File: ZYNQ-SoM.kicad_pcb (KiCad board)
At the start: 6 copper layers, 50 x 40 mm, 173 parts, among them IC501 TPS51206DSQR, J401 AXK500137YG, J402 AXK500137YG, Q201 MMBT3904, U201 xc7z010clg400, U202 W25Q256FVEI, U301 MT41K256M16TW-107_P, U501 TPS62130ARGTR, U502 TPS62130ARGTR, U503 SPX3819M5-L-3-3, U504 TPS62130ARGTR, U701 33.3333MHz

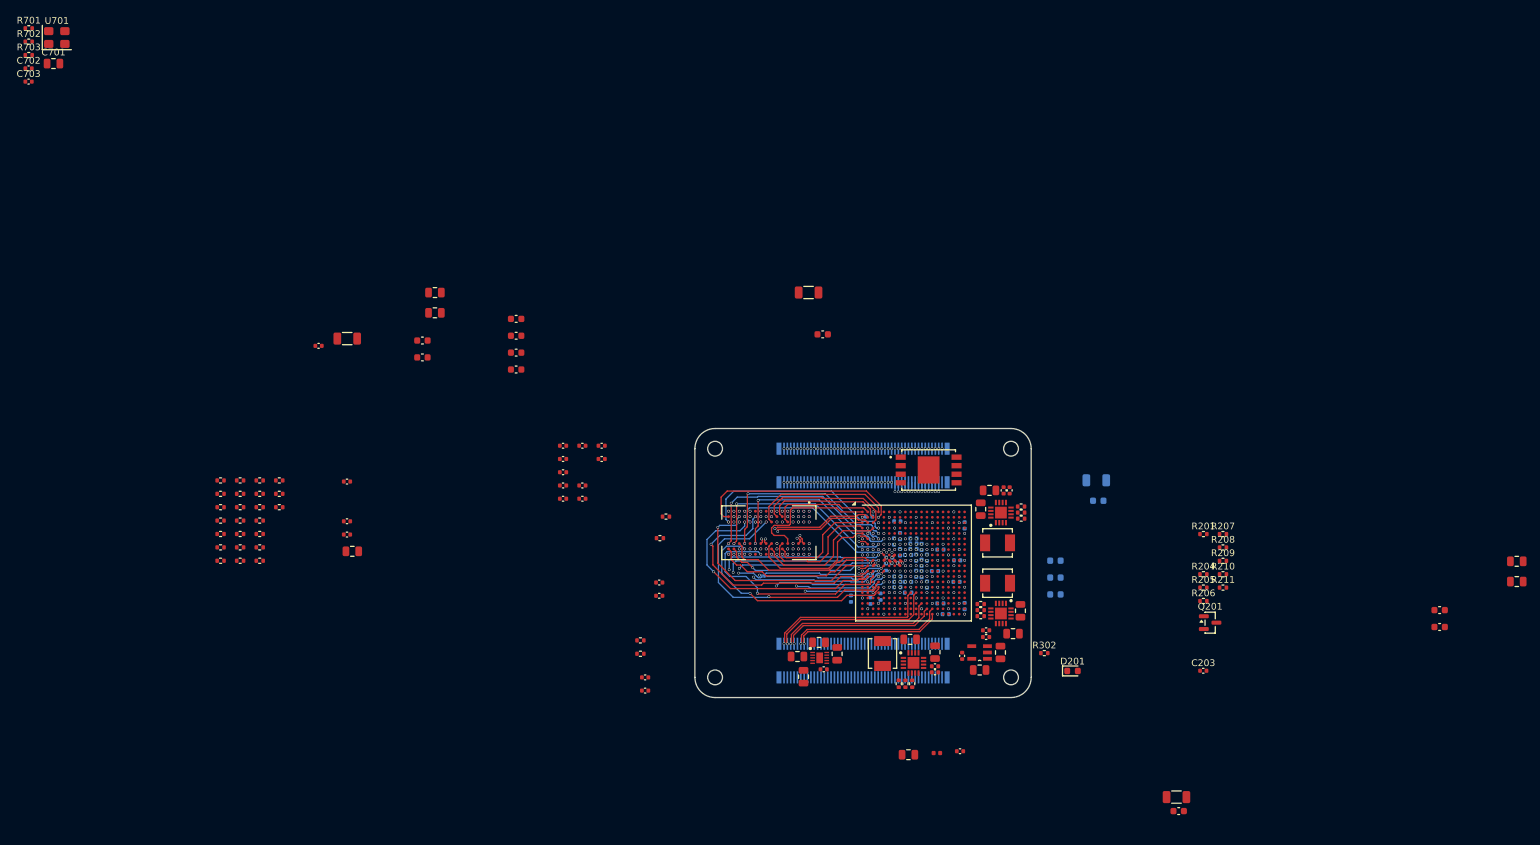
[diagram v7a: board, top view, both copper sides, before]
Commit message: layout: route mio and some io
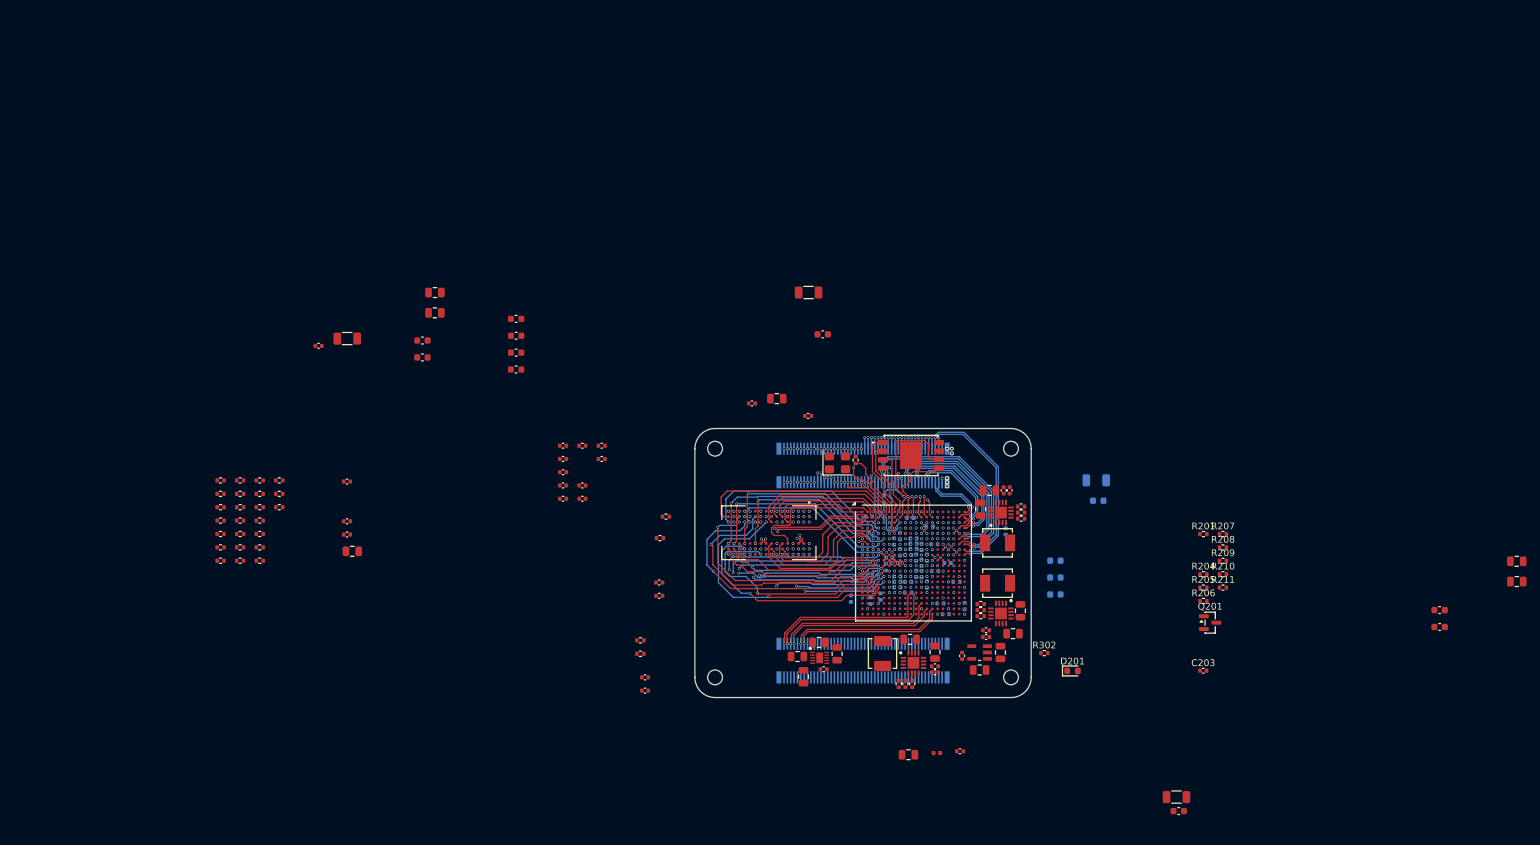
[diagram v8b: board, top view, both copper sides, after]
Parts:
- R701, R703: moved to B.Cu
- moved R703 151.2 mm to (134.9, 74.6)
- moved R701 145.1 mm to (128.1, 70.5), turned to -90 degrees
- moved R702 137.8 mm to (123.9, 64.7), turned to -90 degrees
- moved U701 132.2 mm to (121.2, 65.1)
- moved C703 126.1 mm to (116.8, 58.1)
- moved C701 118.5 mm to (112.2, 55.6)
- moved C702 118.5 mm to (108.5, 56.3)
- moved C565 6.17 mm to (146.2, 75.3)
- moved U202 3.40 mm to (132.1, 64.0)
- moved C551 1.96 mm to (132.0, 73.3)
- moved C559 1.48 mm to (137.6, 80.0)
- moved C571 1.20 mm to (135.6, 77.2)
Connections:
- J402 pad 10: unconnected-(J402-Pad10) -> GND
- J402 pad 100: unconnected-(J402-Pad100) -> GND
- J402 pad 11: unconnected-(J402-Pad11) -> PL_B35_IO1_N
- J402 pad 13: unconnected-(J402-Pad13) -> PL_B35_IO1_P
- J402 pad 15: unconnected-(J402-Pad15) -> GND
- J402 pad 16: unconnected-(J402-Pad16) -> GND
- J402 pad 17: unconnected-(J402-Pad17) -> PL_B35_IO4_P
- J402 pad 19: unconnected-(J402-Pad19) -> PL_B35_IO4_N
- J402 pad 21: unconnected-(J402-Pad21) -> GND
- J402 pad 22: unconnected-(J402-Pad22) -> GND
- J402 pad 23: unconnected-(J402-Pad23) -> PL_B35_IO15_P
- J402 pad 25: unconnected-(J402-Pad25) -> PL_B35_IO15_N
- J402 pad 27: unconnected-(J402-Pad27) -> GND
- J402 pad 28: unconnected-(J402-Pad28) -> GND
- J402 pad 33: unconnected-(J402-Pad33) -> GND
- J402 pad 34: unconnected-(J402-Pad34) -> GND
- J402 pad 35: unconnected-(J402-Pad35) -> PL_B35_IO18_P
- J402 pad 37: unconnected-(J402-Pad37) -> PL_B35_IO18_N
- J402 pad 39: unconnected-(J402-Pad39) -> GND
- J402 pad 40: unconnected-(J402-Pad40) -> GND
- J402 pad 41: unconnected-(J402-Pad41) -> UART_TX
- J402 pad 43: unconnected-(J402-Pad43) -> UART_RX
- J402 pad 45: unconnected-(J402-Pad45) -> GND
- J402 pad 46: unconnected-(J402-Pad46) -> GND
- J402 pad 47: unconnected-(J402-Pad47) -> PS_MIO47
- J402 pad 49: unconnected-(J402-Pad49) -> PS_MIO48
- J402 pad 5: unconnected-(J402-Pad5) -> PL_B35_IO2_P
- J402 pad 51: unconnected-(J402-Pad51) -> GND
- J402 pad 52: unconnected-(J402-Pad52) -> GND
- J402 pad 53: unconnected-(J402-Pad53) -> I2C0_SDA
- J402 pad 55: unconnected-(J402-Pad55) -> I2C0_SCL
- J402 pad 57: unconnected-(J402-Pad57) -> GND
- J402 pad 58: unconnected-(J402-Pad58) -> GND
- J402 pad 59: unconnected-(J402-Pad59) -> PS_MIO9
- J402 pad 6: unconnected-(J402-Pad6) -> PL_B35_IO17_N
- J402 pad 61: unconnected-(J402-Pad61) -> SD_DATA1
- J402 pad 63: unconnected-(J402-Pad63) -> GND
- J402 pad 64: unconnected-(J402-Pad64) -> GND
- J402 pad 65: unconnected-(J402-Pad65) -> SD_DATA3
- J402 pad 67: unconnected-(J402-Pad67) -> SD_CMD
- J402 pad 69: unconnected-(J402-Pad69) -> GND
- J402 pad 7: unconnected-(J402-Pad7) -> PL_B35_IO2_N
- J402 pad 70: unconnected-(J402-Pad70) -> GND
- J402 pad 71: unconnected-(J402-Pad71) -> SD_CLK
- J402 pad 73: unconnected-(J402-Pad73) -> SD_DATA0
- J402 pad 75: unconnected-(J402-Pad75) -> GND
- J402 pad 76: unconnected-(J402-Pad76) -> GND
- J402 pad 77: unconnected-(J402-Pad77) -> SD_DATA2
- J402 pad 79: unconnected-(J402-Pad79) -> OTG_DATA0
- J402 pad 8: unconnected-(J402-Pad8) -> PL_B35_IO17_P
- J402 pad 81: unconnected-(J402-Pad81) -> GND
- J402 pad 82: unconnected-(J402-Pad82) -> GND
- J402 pad 83: unconnected-(J402-Pad83) -> OTG_DATA6
- J402 pad 84: unconnected-(J402-Pad84) -> OTG_DATA7
- J402 pad 85: unconnected-(J402-Pad85) -> OTG_DIR
- J402 pad 86: unconnected-(J402-Pad86) -> OTG_nRST
- J402 pad 87: unconnected-(J402-Pad87) -> GND
- J402 pad 88: unconnected-(J402-Pad88) -> GND
- J402 pad 89: unconnected-(J402-Pad89) -> OTG_DATA2
- J402 pad 9: unconnected-(J402-Pad9) -> GND
- J402 pad 90: unconnected-(J402-Pad90) -> OTG_NXT
- J402 pad 91: unconnected-(J402-Pad91) -> OTG_DATA5
- J402 pad 92: unconnected-(J402-Pad92) -> OTG_DATA4
- J402 pad 93: unconnected-(J402-Pad93) -> GND
- J402 pad 94: unconnected-(J402-Pad94) -> GND
- J402 pad 95: unconnected-(J402-Pad95) -> OTG_CLK
- J402 pad 96: unconnected-(J402-Pad96) -> OTG_STP
- J402 pad 97: unconnected-(J402-Pad97) -> OTG_DATA3
- J402 pad 98: unconnected-(J402-Pad98) -> OTG_DATA1
- J402 pad 99: unconnected-(J402-Pad99) -> GND
- U201 pad B13: PS_MIO50 -> I2C0_SCL
- U201 pad B9: PS_MIO51 -> I2C0_SDA
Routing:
- net unconnected-(J402-Pad48): track 0.00 -> 37.7 mm
- net unconnected-(J402-Pad50): track 0.00 -> 37.7 mm
- net unconnected-(J402-Pad74): track 0.00 -> 36.2 mm
- net unconnected-(J402-Pad72): track 0.00 -> 36.2 mm
- net unconnected-(J402-Pad60): track 0.00 -> 35.8 mm
- net unconnected-(J402-Pad62): track 0.00 -> 35.6 mm
- net unconnected-(J402-Pad66): track 0.00 -> 35.6 mm
- net unconnected-(J402-Pad68): track 0.00 -> 35.6 mm
- net unconnected-(J402-Pad56): track 0.00 -> 35.6 mm
- net unconnected-(J402-Pad54): track 0.00 -> 35.6 mm
- net unconnected-(J402-Pad78): track 0.00 -> 34.3 mm
- net unconnected-(J402-Pad80): track 0.00 -> 34.1 mm
- net PL_B35_IO18_N: track 0.00 -> 34.0 mm, vias 0 -> 2
- net PL_B35_IO18_P: track 0.00 -> 33.4 mm, vias 0 -> 2
- net OTG_NXT: track 0.00 -> 32.3 mm, vias 0 -> 2
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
